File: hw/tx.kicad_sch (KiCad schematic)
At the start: 53 parts, among them Q301 MMBF170, Q302 MMBF170, Q303 MMBF170, Q304 MMBF170, Q305 MMBF170, Q306 MMBF170, Q307 MMBF170, Q308 MMBF170, T301 BN-43-202_DualPri_CTSec, U301 SN74LVC1G74DCTR, U302 UCC27525DGN, U303 UCC27525DGN, U304 Si5351C-B-GM, Y301 40MHz

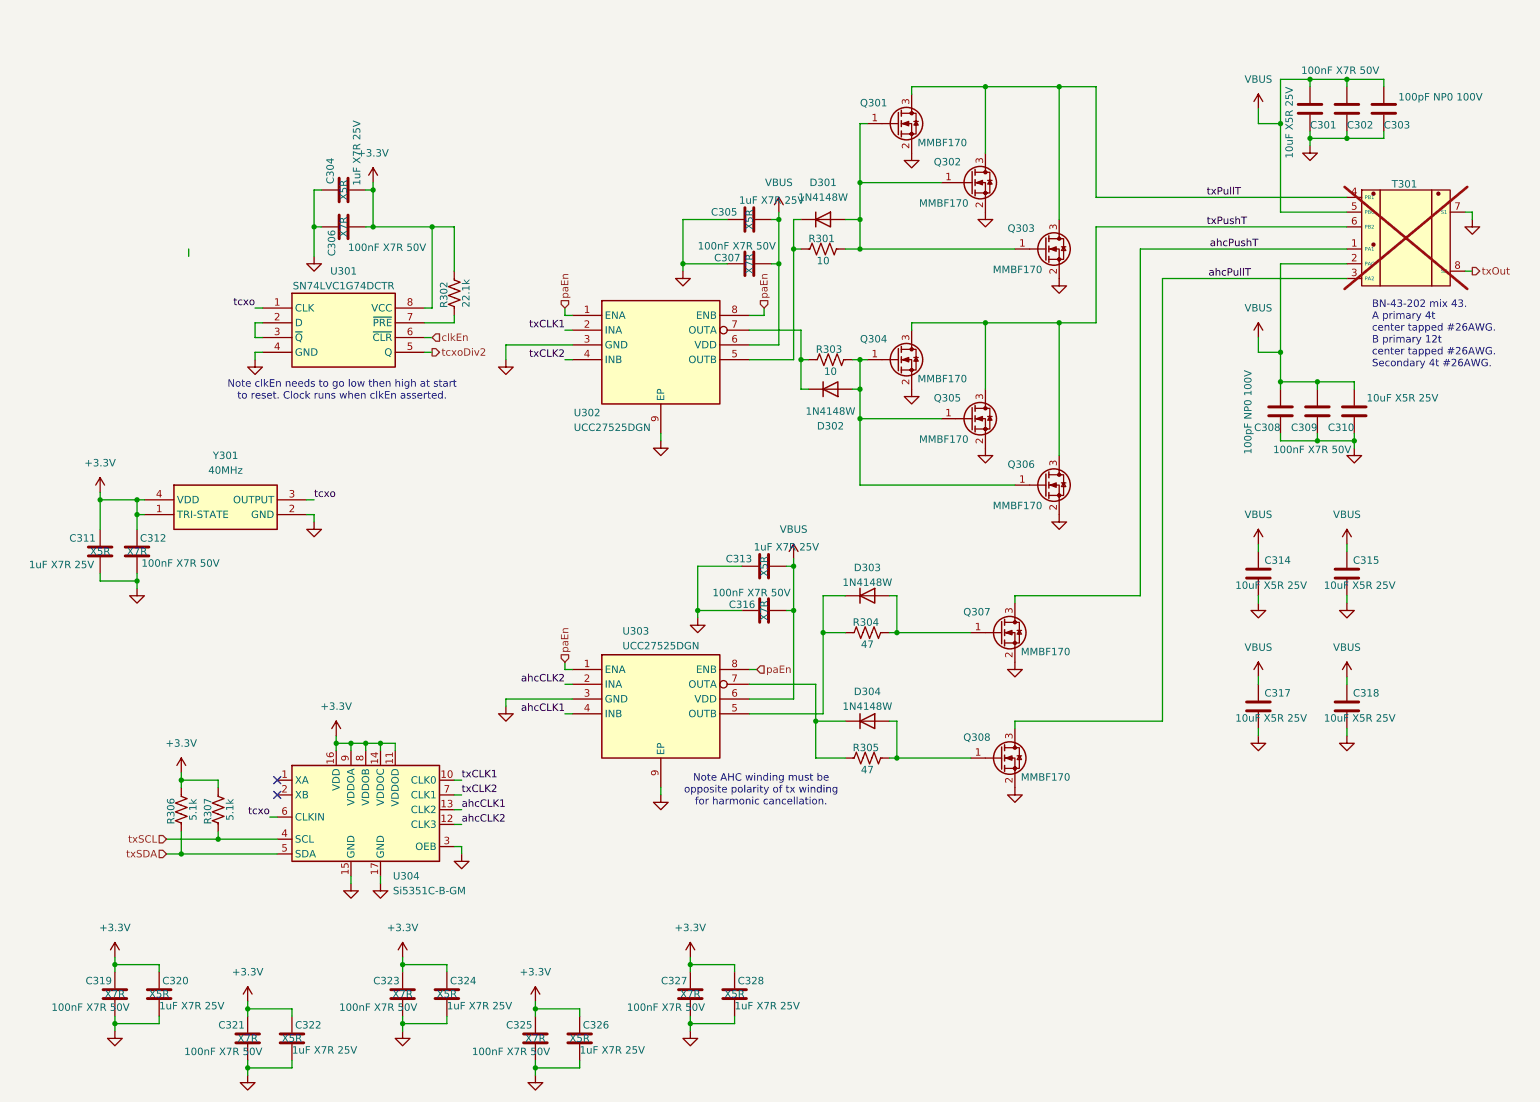
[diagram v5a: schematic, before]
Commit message: Horsing around with JLCPCB assembly and BOM. I think it is still too expensive to do it this way for p1 build
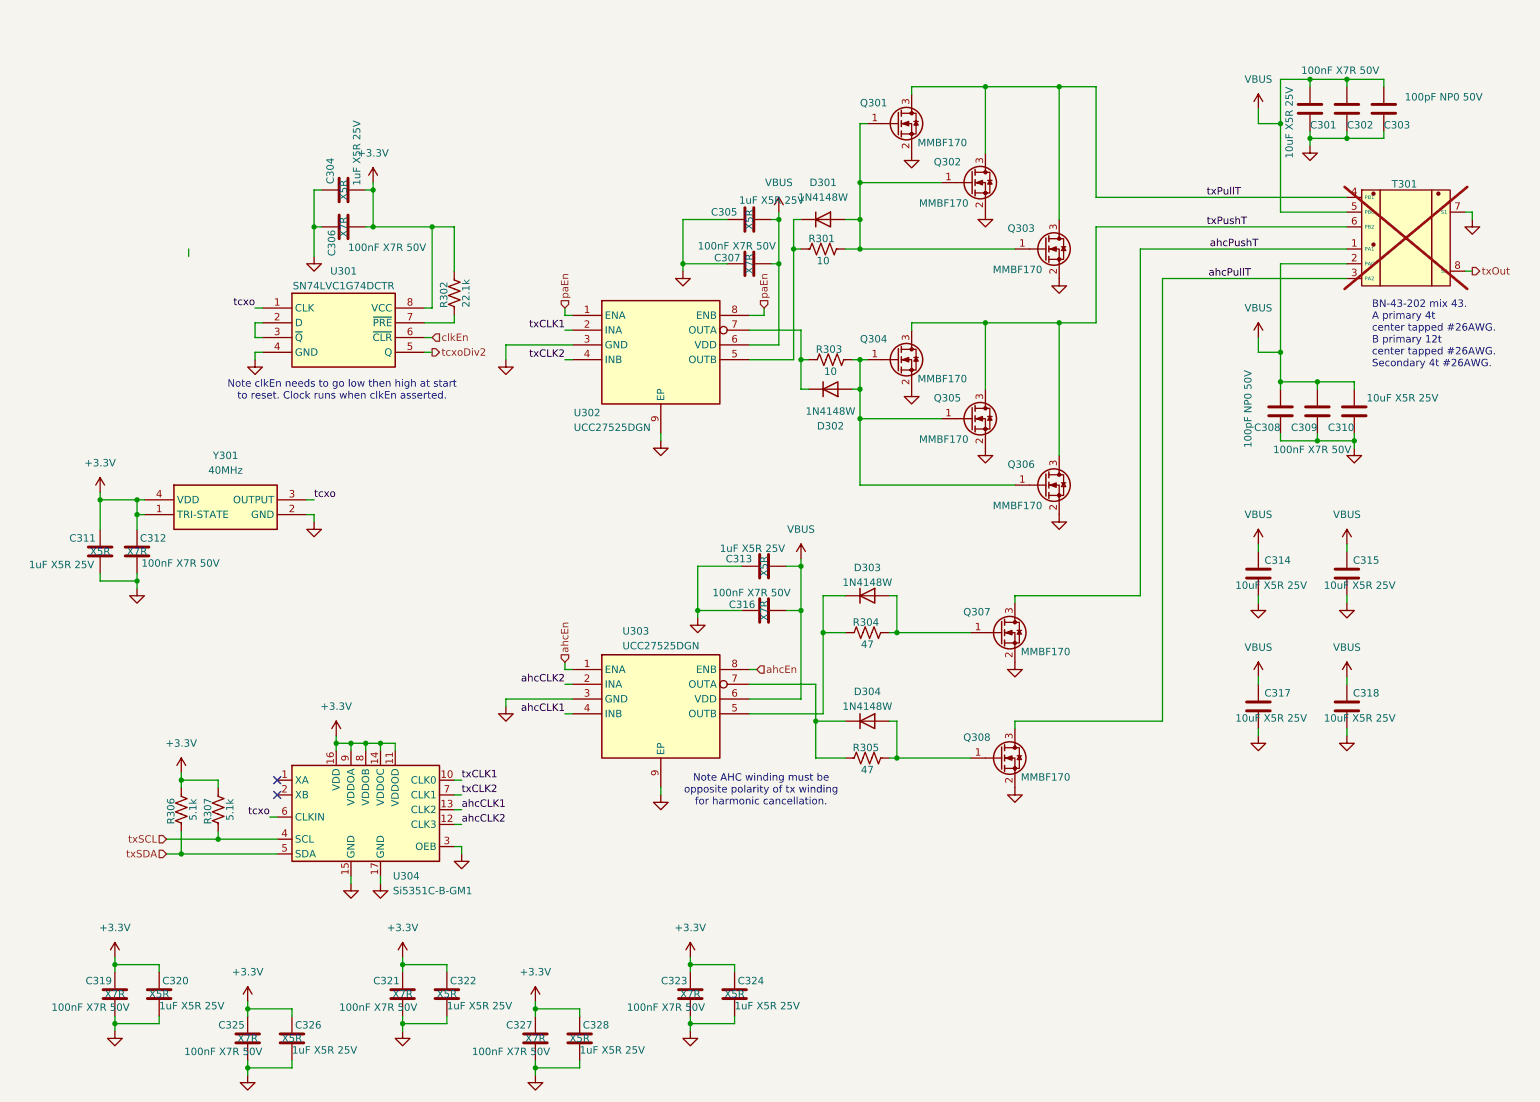
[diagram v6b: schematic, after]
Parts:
- C301, C310, C314, C315, C317, C318: LCSC C96446 -> C479655; cap-type (none) -> X5R
- C302, C307, C309, C316, C319: LCSC C24452 -> C14663
- C303, C308: value 100pF NP0 100V -> 100pF NP0 50V; LCSC C106200 -> C76709; cap-type (none) -> NP0; working-voltage (none) -> 50V
- C304, C305, C311, C313, C320: value 1uF X7R 25V -> 1uF X5R 25V; LCSC C14445 -> C7393852; LCSC_PN C301928 -> (none)
- C306, C312: LCSC C24452 -> C14663; LCSC_PN C24452 -> (none)
- C321: renamed from C323; LCSC C24452 -> C14663
- C322: renamed from C324; value 1uF X7R 25V -> 1uF X5R 25V; LCSC C14445 -> C7393852; LCSC_PN C301928 -> (none)
- C323: renamed from C327; LCSC C24452 -> C14663
- C324: renamed from C328; value 1uF X7R 25V -> 1uF X5R 25V; LCSC C14445 -> C7393852; LCSC_PN C301928 -> (none)
- C325: renamed from C321; LCSC C24452 -> C14663
- C326: renamed from C322; value 1uF X7R 25V -> 1uF X5R 25V; LCSC C14445 -> C7393852; LCSC_PN C301928 -> (none)
- C327: renamed from C325; LCSC C24452 -> C14663
- C328: renamed from C326; value 1uF X7R 25V -> 1uF X5R 25V; LCSC C14445 -> C7393852; LCSC_PN C301928 -> (none)
- D301, D302, D303, D304: LCSC (none) -> C51953478
- Q301, Q302, Q303, Q304, Q305, Q306, Q307, Q308: LCSC C28871 -> C151058
- R301, R303: LCSC C2907091 -> C2784788
- R302: LCSC C2907091 -> C2929993
- R304, R305: LCSC C2907091 -> C2479306
- R306, R307: LCSC C2907091 -> C2906874
- U301: footprint Library:SOP65P400X130-8N -> Package_SO:TSSOP-8_3x3mm_P0.65mm; LCSC (none) -> C52121053; Manufacturer_Name Texas Instruments -> (none); Manufacturer_Part_Number SN74LVC1G74DCTR -> (none); Mouser Part Number 595-SN74LVC1G74DCTR -> (none); Mouser Price/Stock https://www.mouser.co.uk/ProductDetail/Texas-Instruments/SN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 -> (none)
- U302, U303: LCSC (none) -> C2653789
- U304: value Si5351C-B-GM -> Si5351C-B-GM1; MFG (none) -> Skyworks; MPN (none) -> SI5351C-B-GM1; Mouser_PN (none) -> 634-SI5351C-B-GM1
- Y301: LCSC_PN C2451471 -> (none)
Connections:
- net paEn: no longer U303.1 (ENA), U303.8 (ENB)
- new net ahcEn: U303.1 (ENA), U303.8 (ENB)

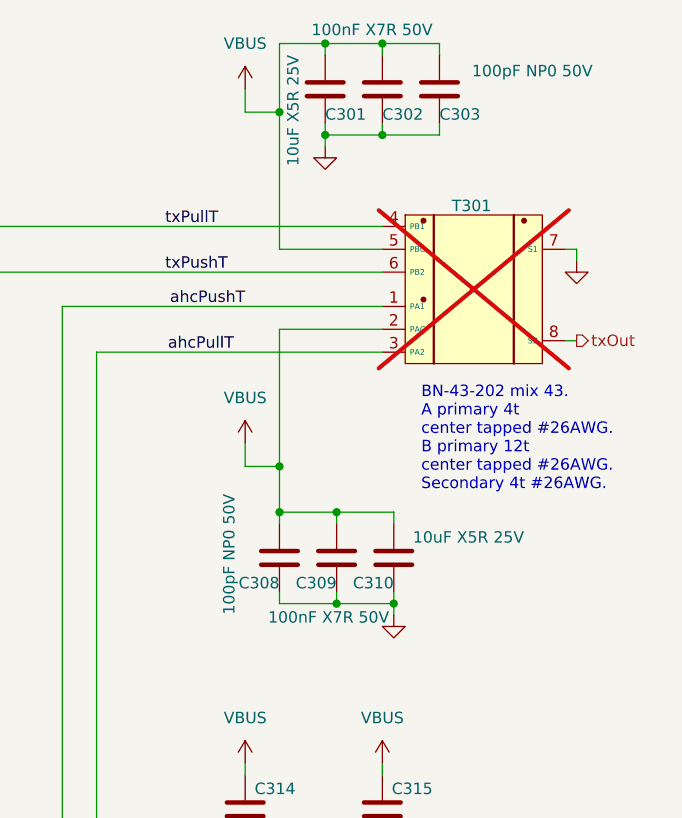
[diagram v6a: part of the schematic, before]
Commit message: OCD fixes. Fix USB2 connector footprint AGAIN (these things are not standardized!).
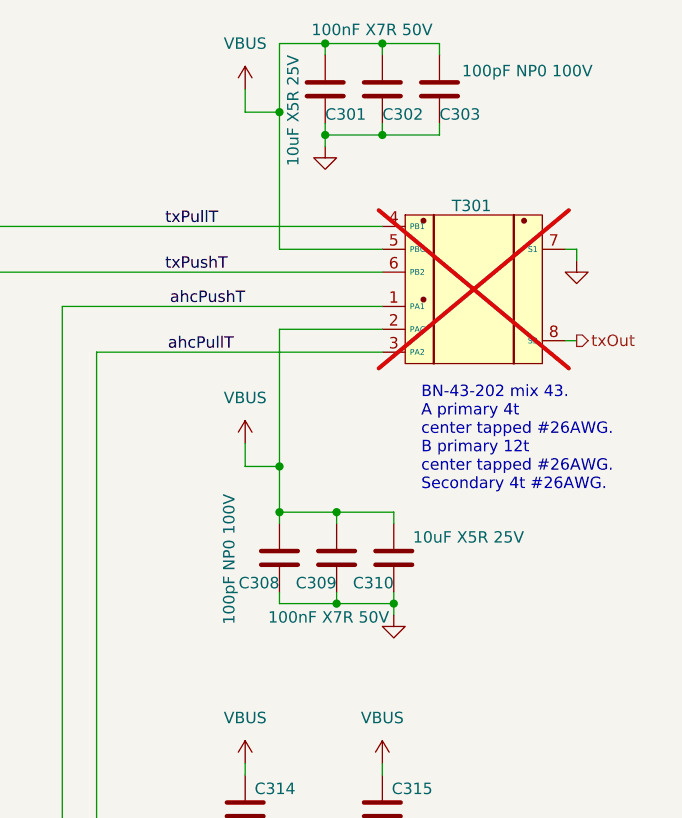
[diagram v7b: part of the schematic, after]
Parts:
- C303, C308: value 100pF NP0 50V -> 100pF NP0 100V
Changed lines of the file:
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@@
 			)
 		)
-		(property "Value" "100pF NP0 50V"
+		(property "Value" "100pF NP0 100V"
 			(at 220.472 74.168 90)
 			(effects
@@
 			)
 		)
-		(property "Value" "100pF NP0 50V"
+		(property "Value" "100pF NP0 100V"
 			(at 260.858 27.178 0)
 			(effects
